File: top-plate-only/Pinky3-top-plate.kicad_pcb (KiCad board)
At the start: 2 copper layers, 135.7 x 77.9 mm, 7 parts

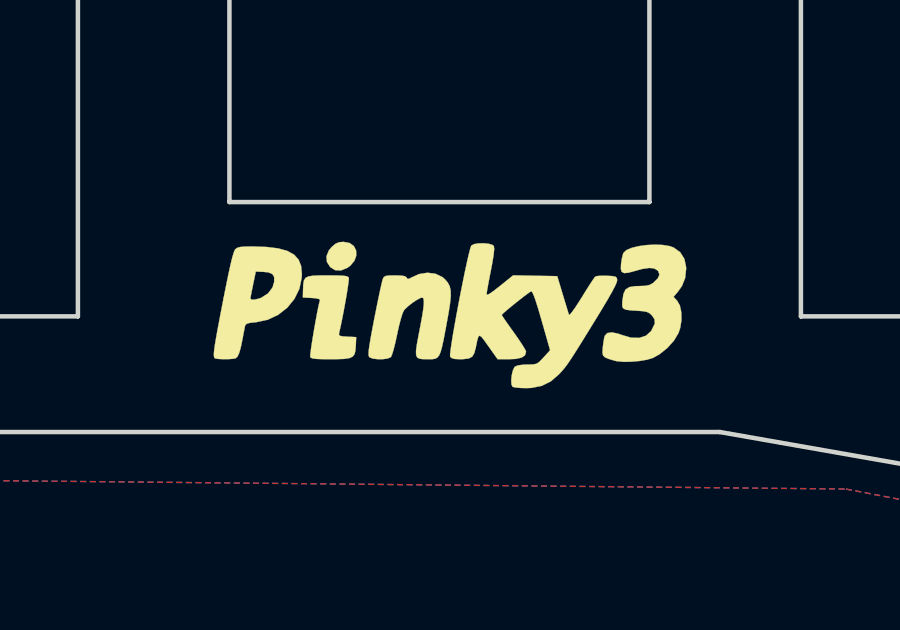
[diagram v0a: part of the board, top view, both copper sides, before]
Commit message: add plates dxf.
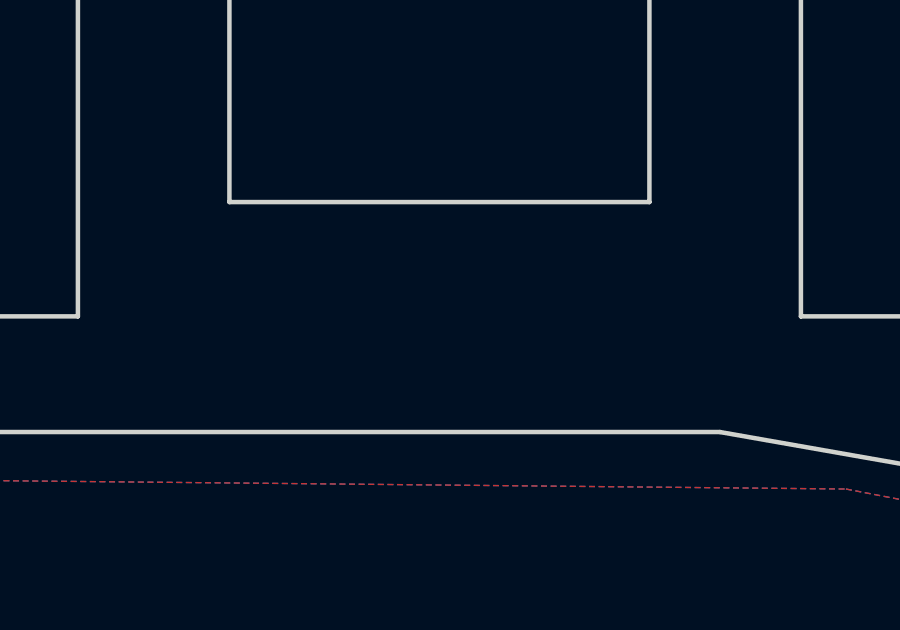
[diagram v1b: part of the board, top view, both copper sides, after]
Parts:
- removed G*** (x2): LOGO, lib:pinky3
